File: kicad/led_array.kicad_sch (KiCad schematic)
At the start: 181 parts, among them Q1 BC807, U4 74HC154BQ,118, U6 LFE5U-85F-6BG381x

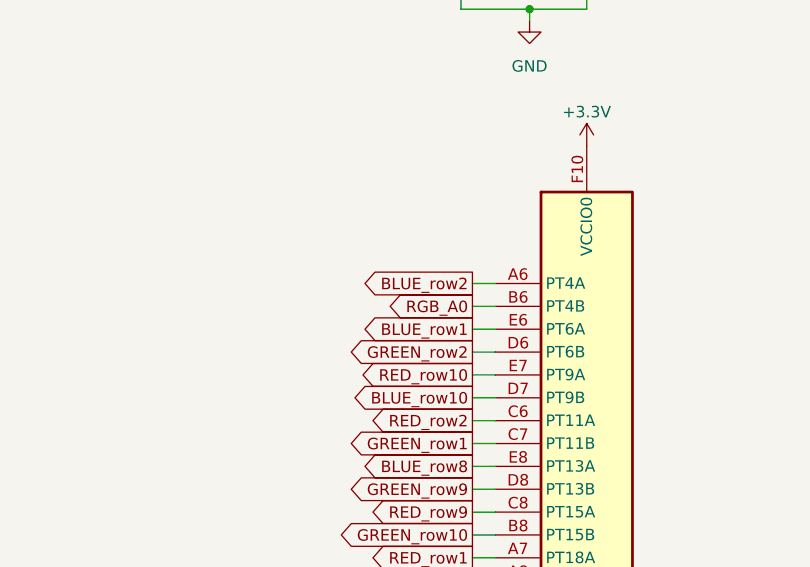
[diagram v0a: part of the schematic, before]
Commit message: Removed the nDet from the SD-card and added the 12 MHz oscillator as clock input to be fully compatible with the GECKO4 clock inputs
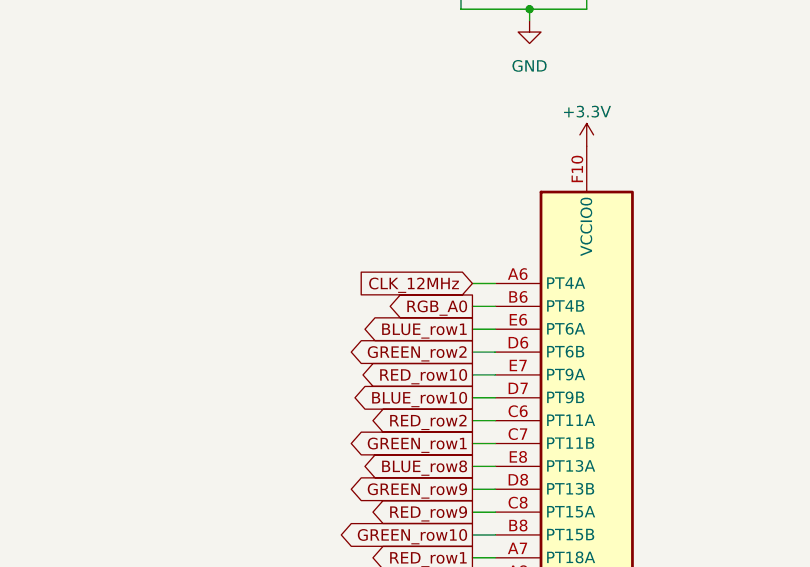
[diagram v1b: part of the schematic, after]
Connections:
- net BLUE_row2: no longer U6.A6 (PT4A)
- new net CLK_12MHz: U6.A6 (PT4A)
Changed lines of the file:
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@@
-    )
-  )
-  (global_label "BLUE_row2" (shape output) (at 318.77 151.13 180) (fields_autoplaced)
-    (effects (font (size 1.27 1.27)) (justify right))
-    (property "Intersheetrefs" "${INTERSHEET_REFS}" (at 305.6438 151.13 0)
-      (effects (font (size 1.27 1.27)) (justify right) hide)
     )
   )
@@
     )
   )
+  (global_label "CLK_12MHz" (shape input) (at 318.77 151.13 180) (fields_autoplaced)
+    (effects (font (size 1.27 1.27)) (justify right))
+    (property "Intersheetrefs" "${INTERSHEET_REFS}" (at 305.0995 151.13 0)
+      (effects (font (size 1.27 1.27)) (justify right) hide)
+    )
+  )
